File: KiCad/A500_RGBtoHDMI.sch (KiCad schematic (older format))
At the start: 13 parts, among them J1 Conn_02x20_Odd_Even, U1 Denise_Socket, U2 XC9572XL-VQ64, U3 LM1117-3.3, U4 Denise_MB_PinHeader

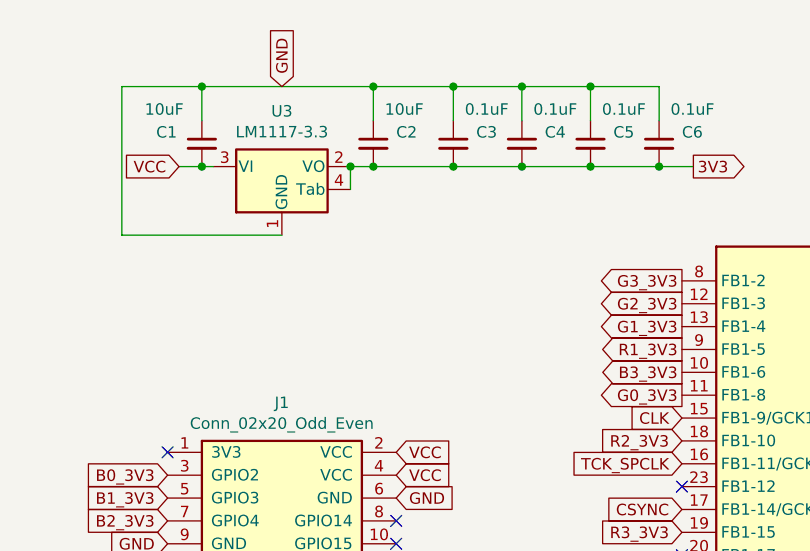
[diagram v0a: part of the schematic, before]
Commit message: added a two-pin power header VCC/GND
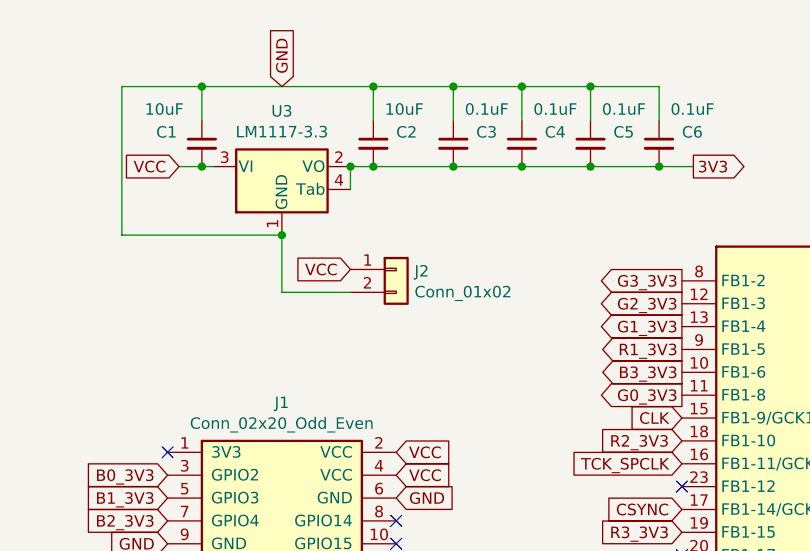
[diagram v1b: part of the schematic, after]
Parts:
- added J2: Conn_01x02, Connector_PinHeader_2.00mm:PinHeader_1x02_P2.00mm_Vertical, symbol Connector_Generic:Conn_01x02
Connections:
- net +5V: now also J2.1 (Pin_1)
- net GND: now also J2.2 (Pin_2)
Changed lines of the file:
@@
 	8600 850  8300 850
 Connection ~ 8300 850
+$Comp
+L Connector_Generic:Conn_01x02 J2
+U 1 1 624ED77D
+P 7450 1650
+F 0 "J2" H 7530 1642 50  0000 L CNN
+F 1 "Conn_01x02" H 7530 1551 50  0000 L CNN
+F 2 "Connector_PinHeader_2.00mm:PinHeader_1x02_P2.00mm_Vertical" H 7450 1650 50  0001 C CNN
+F 3 "~" H 7450 1650 50  0001 C CNN
+	1    7450 1650
+	1    0    0    -1
+$EndComp
+Text GLabel 7250 1650 0    50   Input ~ 0
+VCC
+Wire Wire Line
+	7250 1750 6950 1750
+Wire Wire Line
+	6950 1750 6950 1500
+Connection ~ 6950 1500
 $EndSCHEMATC

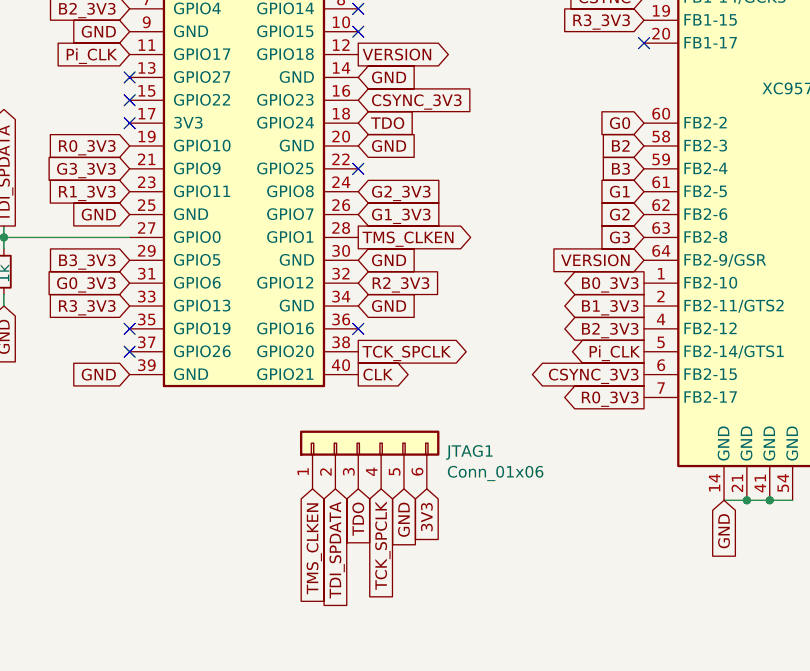
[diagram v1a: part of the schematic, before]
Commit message: added Button-jumper (BT1) with 3V3-pull-up resistor
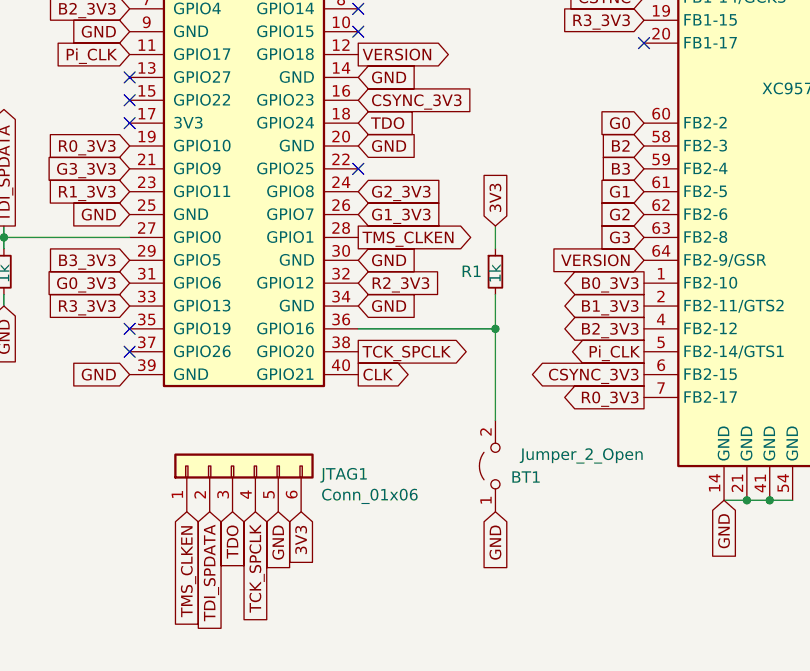
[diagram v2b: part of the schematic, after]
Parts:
- added BT1: Jumper_2_Open, Connector_PinHeader_2.54mm:PinHeader_1x02_P2.54mm_Horizontal, symbol Jumper:Jumper_2_Open
- added R1: 1k, Resistor_SMD:R_0805_2012Metric_Pad1.15x1.40mm_HandSolder, symbol Device:R_Small
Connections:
- net 3V3: now also R1.1
- net GND: now also BT1.1 (A)
- net at J1.36 (GPIO16): now also BT1.2 (B), R1.2
- no-connect marks 30 -> 29
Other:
- moved on the sheet: JTAG1
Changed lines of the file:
@@
 L Connector_Generic:Conn_01x06 JTAG1
 U 1 1 6241CCF9
-P 7450 4650
-F 0 "JTAG1" V 7414 4262 50  0000 R CNN
-F 1 "Conn_01x06" V 7323 4262 50  0000 R CNN
-F 2 "Connector_PinHeader_2.54mm:PinHeader_1x06_P2.54mm_Vertical" H 7450 4650 50  0001 C CNN
-F 3 "~" H 7450 4650 50  0001 C CNN
-	1    7450 4650
+P 6900 4750
+F 0 "JTAG1" V 6864 4362 50  0000 R CNN
+F 1 "Conn_01x06" V 6773 4362 50  0000 R CNN
+F 2 "Connector_PinHeader_2.54mm:PinHeader_1x06_P2.54mm_Vertical" H 6900 4750 50  0001 C CNN
+F 3 "~" H 6900 4750 50  0001 C CNN
+	1    6900 4750
 	0    -1   -1   0
 $EndComp
-Text GLabel 7450 4850 3    50   Input ~ 0
+Text GLabel 6900 4950 3    50   Input ~ 0
 TDO
-Text GLabel 7650 4850 3    50   Input ~ 0
+Text GLabel 7100 4950 3    50   Input ~ 0
 GND
-Text GLabel 7750 4850 3    50   Input ~ 0
+Text GLabel 7200 4950 3    50   Input ~ 0
 3V3
 Text GLabel 9400 1400 1    50   Input ~ 0
@@
 NoConn ~ 6450 4250
 NoConn ~ 6450 4150
-NoConn ~ 7450 4150
 Text GLabel 8700 2400 0    50   Input ~ 0
 R2_3V3
@@
 Text GLabel 5900 3700 1    50   Output ~ 0
 TDI_SPDATA
-Text GLabel 7350 4850 3    50   Input ~ 0
+Text GLabel 6800 4950 3    50   Input ~ 0
 TDI_SPDATA
 Text GLabel 9950 4900 3    50   Input ~ 0
@@
 Text GLabel 7450 3750 2    50   Output ~ 0
 TMS_CLKEN
-Text GLabel 7250 4850 3    50   Input ~ 0
+Text GLabel 6700 4950 3    50   Input ~ 0
 TMS_CLKEN
 Text GLabel 9850 4900 3    50   Input ~ 0
@@
 Text GLabel 10300 1800 2    50   Input ~ 0
 TMS_CLKEN
-Text GLabel 7550 4850 3    50   Input ~ 0
+Text GLabel 7000 4950 3    50   Input ~ 0
 TCK_SPCLK
 Text GLabel 9750 4900 3    50   Input ~ 0
@@
 	7700 850  7350 850
 Connection ~ 7350 850
+Wire Wire Line
+	6450 3750 5900 3750
+Text GLabel 5900 4050 3    50   Input ~ 0
+GND
+Wire Wire Line
+	5900 3700 5900 3750
+Connection ~ 5900 3750
+Wire Wire Line
+	5900 3750 5900 3800
+Wire Wire Line
+	5900 4000 5900 4050
+$Comp
+L Device:C_Small C4
+U 1 1 624DDB45
+P 8000 1100
+F 0 "C4" H 8100 1150 50  0000 L CNN
+F 1 "0.1uF" H 8050 1250 50  0000 L CNN
+F 2 "Capacitor_SMD:C_0805_2012Metric_Pad1.15x1.40mm_HandSolder" H 8000 1100 50  0001 C CNN
+F 3 "~" H 8000 1100 50  0001 C CNN
+	1    8000 1100
+	1    0    0    -1
+$EndComp
+$Comp
+L Device:C_Small C5
+U 1 1 624DE9B4
+P 8300 1100
+F 0 "C5" H 8400 1150 50  0000 L CNN
+F 1 "0.1uF" H 8350 1250 50  0000 L CNN
+F 2 "Capacitor_SMD:C_0805_2012Metric_Pad1.15x1.40mm_HandSolder" H 8300 1100 50  0001 C CNN
+F 3 "~" H 8300 1100 50  0001 C CNN
+	1    8300 1100
+	1    0    0    -1
+$EndComp
+$Comp
+L Device:C_Small C6
+U 1 1 624DF886
+P 8600 1100
+F 0 "C6" H 8700 1150 50  0000 L CNN
+F 1 "0.1uF" H 8650 1250 50  0000 L CNN
+F 2 "Capacitor_SMD:C_0805_2012Metric_Pad1.15x1.40mm_HandSolder" H 8600 1100 50  0001 C CNN
+F 3 "~" H 8600 1100 50  0001 C CNN
+	1    8600 1100
+	1    0    0    -1
+$EndComp
+Wire Wire Line
+	7700 1200 8000 1200
+Connection ~ 8000 1200
+Wire Wire Line
+	8000 1200 8300 1200
+Connection ~ 8300 1200
+Wire Wire Line
+	8300 1200 8600 1200
+Connection ~ 8600 1200
+Wire Wire Line
+	8600 1200 8750 1200
+Wire Wire Line
+	8000 1000 8000 850
+Wire Wire Line
+	8000 850  7700 850
+Connection ~ 7700 850
+Wire Wire Line
+	8300 1000 8300 850
+Wire Wire Line
+	8300 850  8000 850
+Connection ~ 8000 850
+Wire Wire Line
+	8600 1000 8600 850
+Wire Wire Line
+	8600 850  8300 850
+Connection ~ 8300 850
+$Comp
+L Connector_Generic:Conn_01x02 J2
+U 1 1 624ED77D
+P 7450 1650
+F 0 "J2" H 7530 1642 50  0000 L CNN
+F 1 "Conn_01x02" H 7530 1551 50  0000 L CNN
+F 2 "Connector_PinHeader_2.00mm:PinHeader_1x02_P2.00mm_Vertical" H 7450 1650 50  0001 C CNN
+F 3 "~" H 7450 1650 50  0001 C CNN
+	1    7450 1650
+	1    0    0    -1
+$EndComp
+Text GLabel 7250 1650 0    50   Input ~ 0
+VCC
+Wire Wire Line
+	7250 1750 6950 1750
+Wire Wire Line
+	6950 1750 6950 1500
+Connection ~ 6950 1500
+Wire Wire Line
+	7450 4150 8050 4150
+Wire Wire Line
+	8050 4150 8050 4000
+Text GLabel 8050 3700 1    50   Input ~ 0
+3V3
+Wire Wire Line
+	8050 3800 8050 3700
 $Comp
 L Device:R_Small R2
@@
 	1    0    0    -1
 $EndComp
-Wire Wire Line
-	6450 3750 5900 3750
-Text GLabel 5900 4050 3    50   Input ~ 0
+$Comp
+L Device:R_Small R1
+U 1 1 624FD62F
+P 8050 3900
+F 0 "R1" H 7900 3900 50  0000 L CNN
+F 1 "1k" V 8050 3850 50  0000 L CNN
+F 2 "Resistor_SMD:R_0805_2012Metric_Pad1.15x1.40mm_HandSolder" H 8050 3900 50  0001 C CNN
+F 3 "~" H 8050 3900 50  0001 C CNN
+	1    8050 3900
+	1    0    0    -1
+$EndComp
+Text GLabel 8050 4950 3    50   Input ~ 0
 GND
 Wire Wire Line
-	5900 3700 5900 3750
-Connection ~ 5900 3750
-Wire Wire Line
-	5900 3750 5900 3800
-Wire Wire Line
-	5900 4000 5900 4050
-$Comp
-L Device:C_Small C4
-U 1 1 624DDB45
-P 8000 1100
-F 0 "C4" H 8100 1150 50  0000 L CNN
-F 1 "0.1uF" H 8050 1250 50  0000 L CNN
-F 2 "Capacitor_SMD:C_0805_2012Metric_Pad1.15x1.40mm_HandSolder" H 8000 1100 50  0001 C CNN
-F 3 "~" H 8000 1100 50  0001 C CNN
-	1    8000 1100
-	1    0    0    -1
-$EndComp
-$Comp
-L Device:C_Small C5
-U 1 1 624DE9B4
-P 8300 1100
-F 0 "C5" H 8400 1150 50  0000 L CNN
-F 1 "0.1uF" H 8350 1250 50  0000 L CNN
-F 2 "Capacitor_SMD:C_0805_2012Metric_Pad1.15x1.40mm_HandSolder" H 8300 1100 50  0001 C CNN
-F 3 "~" H 8300 1100 50  0001 C CNN
-	1    8300 1100
-	1    0    0    -1
-$EndComp
-$Comp
-L Device:C_Small C6
-U 1 1 624DF886
-P 8600 1100
-F 0 "C6" H 8700 1150 50  0000 L CNN
-F 1 "0.1uF" H 8650 1250 50  0000 L CNN
-F 2 "Capacitor_SMD:C_0805_2012Metric_Pad1.15x1.40mm_HandSolder" H 8600 1100 50  0001 C CNN
-F 3 "~" H 8600 1100 50  0001 C CNN
-	1    8600 1100
-	1    0    0    -1
-$EndComp
-Wire Wire Line
-	7700 1200 8000 1200
-Connection ~ 8000 1200
-Wire Wire Line
-	8000 1200 8300 1200
-Connection ~ 8300 1200
-Wire Wire Line
-	8300 1200 8600 1200
-Connection ~ 8600 1200
-Wire Wire Line
-	8600 1200 8750 1200
-Wire Wire Line
-	8000 1000 8000 850
-Wire Wire Line
-	8000 850  7700 850
-Connection ~ 7700 850
-Wire Wire Line
-	8300 1000 8300 850
-Wire Wire Line
-	8300 850  8000 850
-Connection ~ 8000 850
-Wire Wire Line
-	8600 1000 8600 850
-Wire Wire Line
-	8600 850  8300 850
-Connection ~ 8300 850
-$Comp
-L Connector_Generic:Conn_01x02 J2
-U 1 1 624ED77D
-P 7450 1650
-F 0 "J2" H 7530 1642 50  0000 L CNN
-F 1 "Conn_01x02" H 7530 1551 50  0000 L CNN
-F 2 "Connector_PinHeader_2.00mm:PinHeader_1x02_P2.00mm_Vertical" H 7450 1650 50  0001 C CNN
-F 3 "~" H 7450 1650 50  0001 C CNN
-	1    7450 1650
-	1    0    0    -1
-$EndComp
-Text GLabel 7250 1650 0    50   Input ~ 0
-VCC
-Wire Wire Line
-	7250 1750 6950 1750
-Wire Wire Line
-	6950 1750 6950 1500
-Connection ~ 6950 1500
+	8050 4150 8050 4550
+Connection ~ 8050 4150
+$Comp
+L Jumper:Jumper_2_Open BT1
+U 1 1 62508B6C
+P 8050 4750
+F 0 "BT1" V 8000 4550 50  0000 L CNN
+F 1 "Jumper_2_Open" V 8100 4100 50  0000 L CNN
+F 2 "Connector_PinHeader_2.54mm:PinHeader_1x02_P2.54mm_Horizontal" H 8050 4750 50  0001 C CNN
+F 3 "~" H 8050 4750 50  0001 C CNN
+	1    8050 4750
+	0    -1   -1   0
+$EndComp
 $EndSCHEMATC

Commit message: added DETECT-signal with pull-down resistor
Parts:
- added R3: 4.7k, Resistor_SMD:R_0805_2012Metric_Pad1.15x1.40mm_HandSolder, symbol Device:R_Small
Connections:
- net GND: now also R3.2
- net DETECT: now reaches U2.20 (FB1-17)
- net DETECT: now also R3.1
- no-connect marks 29 -> 28
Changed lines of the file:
@@
 TCK_SPCLK
 NoConn ~ 8700 2600
-NoConn ~ 8700 2900
-NoConn ~ 10300 1700
 NoConn ~ 10300 1900
 NoConn ~ 10300 2000
@@
 	0    -1   -1   0
 $EndComp
+Text GLabel 8300 2900 0    50   Input ~ 0
+DETECT
+NoConn ~ 10300 1700
+$Comp
+L Device:R_Small R3
+U 1 1 6252A94A
+P 8400 3100
+F 0 "R3" H 8250 3100 50  0000 L CNN
+F 1 "4.7k" H 8450 3100 50  0000 L CNN
+F 2 "Resistor_SMD:R_0805_2012Metric_Pad1.15x1.40mm_HandSolder" H 8400 3100 50  0001 C CNN
+F 3 "~" H 8400 3100 50  0001 C CNN
+	1    8400 3100
+	1    0    0    -1
+$EndComp
+Text GLabel 8400 3200 3    50   Input ~ 0
+GND
+Wire Wire Line
+	8700 2900 8400 2900
+Wire Wire Line
+	8400 3000 8400 2900
+Connection ~ 8400 2900
+Wire Wire Line
+	8400 2900 8300 2900
 $EndSCHEMATC

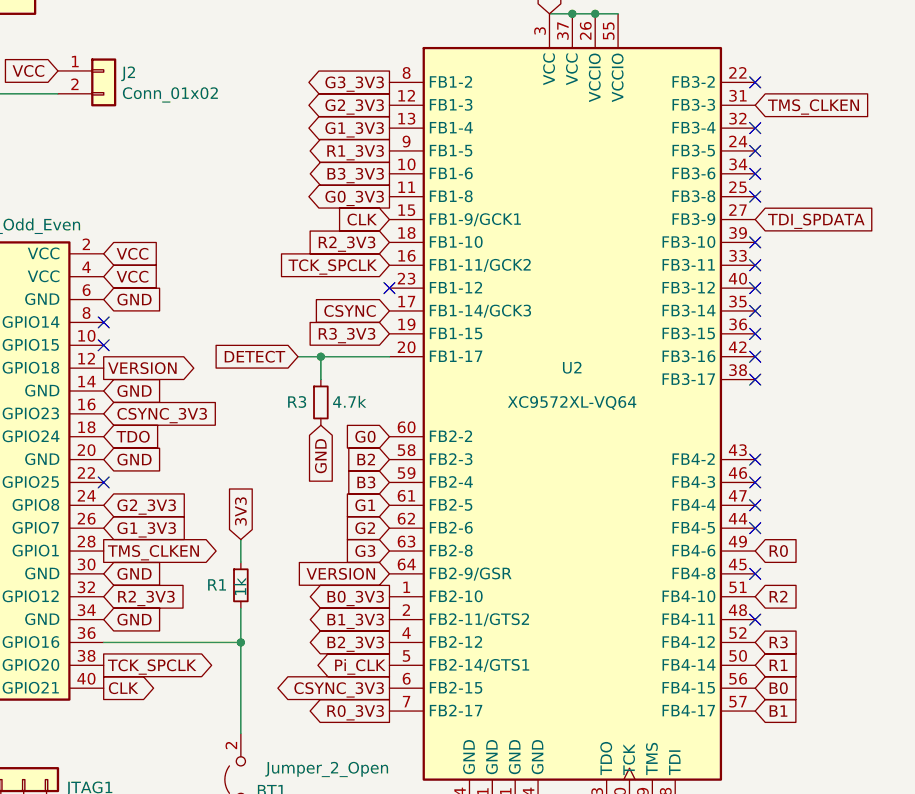
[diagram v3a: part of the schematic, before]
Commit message: add CSYNC-PinHeader for Rev3 A500-mobos
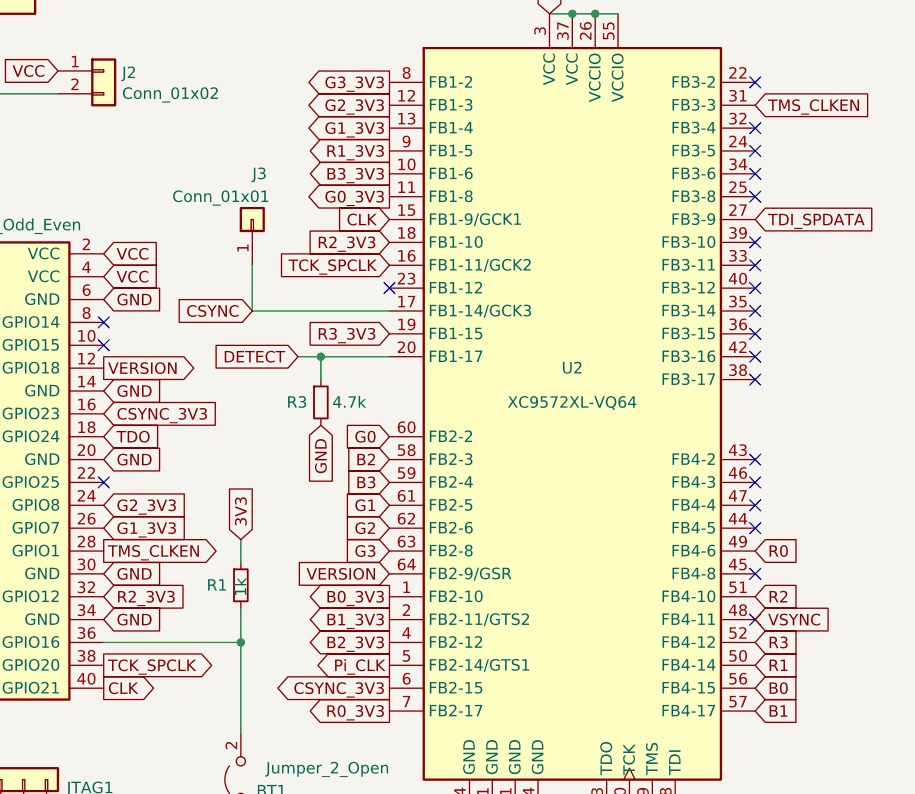
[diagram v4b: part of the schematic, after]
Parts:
- added J3: Conn_01x01, Connector_PinHeader_2.54mm:PinHeader_1x01_P2.54mm_Horizontal, symbol Connector_Generic:Conn_01x01
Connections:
- net CSYNC: now also J3.1 (Pin_1)
- net VSYNC: now reaches U2.48 (FB4-11)
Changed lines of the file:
@@
 Text GLabel 8700 3850 0    50   Input ~ 0
 VERSION
-Text GLabel 8700 2700 0    50   Input ~ 0
+Text GLabel 8100 2700 0    50   Input ~ 0
 CSYNC
 Text GLabel 8700 2100 0    50   Output ~ 0
@@
 NoConn ~ 10300 3650
 NoConn ~ 10300 3850
-NoConn ~ 10300 4050
 $Comp
 L A500_RGBtoHDMI:LM1117-3.3 U3
@@
 Wire Wire Line
 	8400 2900 8300 2900
+NoConn ~ 10300 4050
+Text GLabel 10300 4050 2    50   Input ~ 0
+VSYNC
+$Comp
+L Connector_Generic:Conn_01x01 J3
+U 1 1 62568E0B
+P 8100 2300
+F 0 "J3" V 8300 2300 50  0000 R CNN
+F 1 "Conn_01x01" V 8200 2650 50  0000 R CNN
+F 2 "Connector_PinHeader_2.54mm:PinHeader_1x01_P2.54mm_Horizontal" H 8100 2300 50  0001 C CNN
+F 3 "~" H 8100 2300 50  0001 C CNN
+	1    8100 2300
+	0    -1   -1   0
+$EndComp
+Wire Wire Line
+	8100 2500 8100 2700
+Wire Wire Line
+	8700 2700 8100 2700
 $EndSCHEMATC

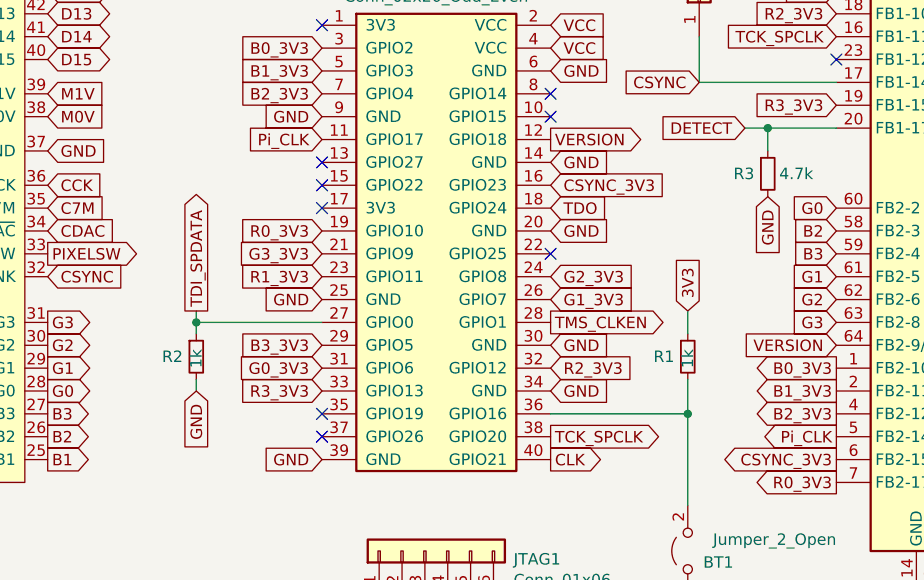
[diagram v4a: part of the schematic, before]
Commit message: removed pull-up resistor on BT1 (gpio16), not needed
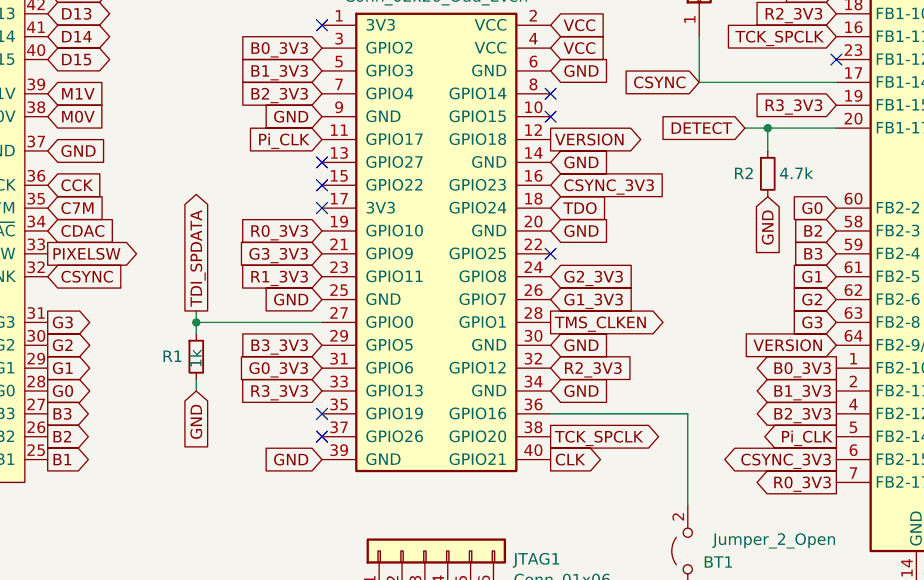
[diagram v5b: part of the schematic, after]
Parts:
- removed R1: 1k, Resistor_SMD:R_0805_2012Metric_Pad1.15x1.40mm_HandSolder, symbol Device:R_Small
- renumbered R2 to R1, R3 to R2
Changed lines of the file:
@@
 Wire Wire Line
 	7450 4150 8050 4150
-Wire Wire Line
-	8050 4150 8050 4000
-Text GLabel 8050 3700 1    50   Input ~ 0
-3V3
-Wire Wire Line
-	8050 3800 8050 3700
 $Comp
-L Device:R_Small R2
+L Device:R_Small R1
 U 1 1 624D6906
 P 5900 3900
-F 0 "R2" H 5750 3900 50  0000 L CNN
+F 0 "R1" H 5750 3900 50  0000 L CNN
 F 1 "1k" V 5900 3850 50  0000 L CNN
 F 2 "Resistor_SMD:R_0805_2012Metric_Pad1.15x1.40mm_HandSolder" H 5900 3900 50  0001 C CNN
@@
 	1    0    0    -1
 $EndComp
-$Comp
-L Device:R_Small R1
-U 1 1 624FD62F
-P 8050 3900
-F 0 "R1" H 7900 3900 50  0000 L CNN
-F 1 "1k" V 8050 3850 50  0000 L CNN
-F 2 "Resistor_SMD:R_0805_2012Metric_Pad1.15x1.40mm_HandSolder" H 8050 3900 50  0001 C CNN
-F 3 "~" H 8050 3900 50  0001 C CNN
-	1    8050 3900
-	1    0    0    -1
-$EndComp
 Text GLabel 8050 4950 3    50   Input ~ 0
 GND
 Wire Wire Line
 	8050 4150 8050 4550
-Connection ~ 8050 4150
 $Comp
 L Jumper:Jumper_2_Open BT1
@@
 NoConn ~ 10300 1700
 $Comp
-L Device:R_Small R3
+L Device:R_Small R2
 U 1 1 6252A94A
 P 8400 3100
-F 0 "R3" H 8250 3100 50  0000 L CNN
+F 0 "R2" H 8250 3100 50  0000 L CNN
 F 1 "4.7k" H 8450 3100 50  0000 L CNN
 F 2 "Resistor_SMD:R_0805_2012Metric_Pad1.15x1.40mm_HandSolder" H 8400 3100 50  0001 C CNN
